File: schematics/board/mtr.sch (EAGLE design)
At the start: 6 parts

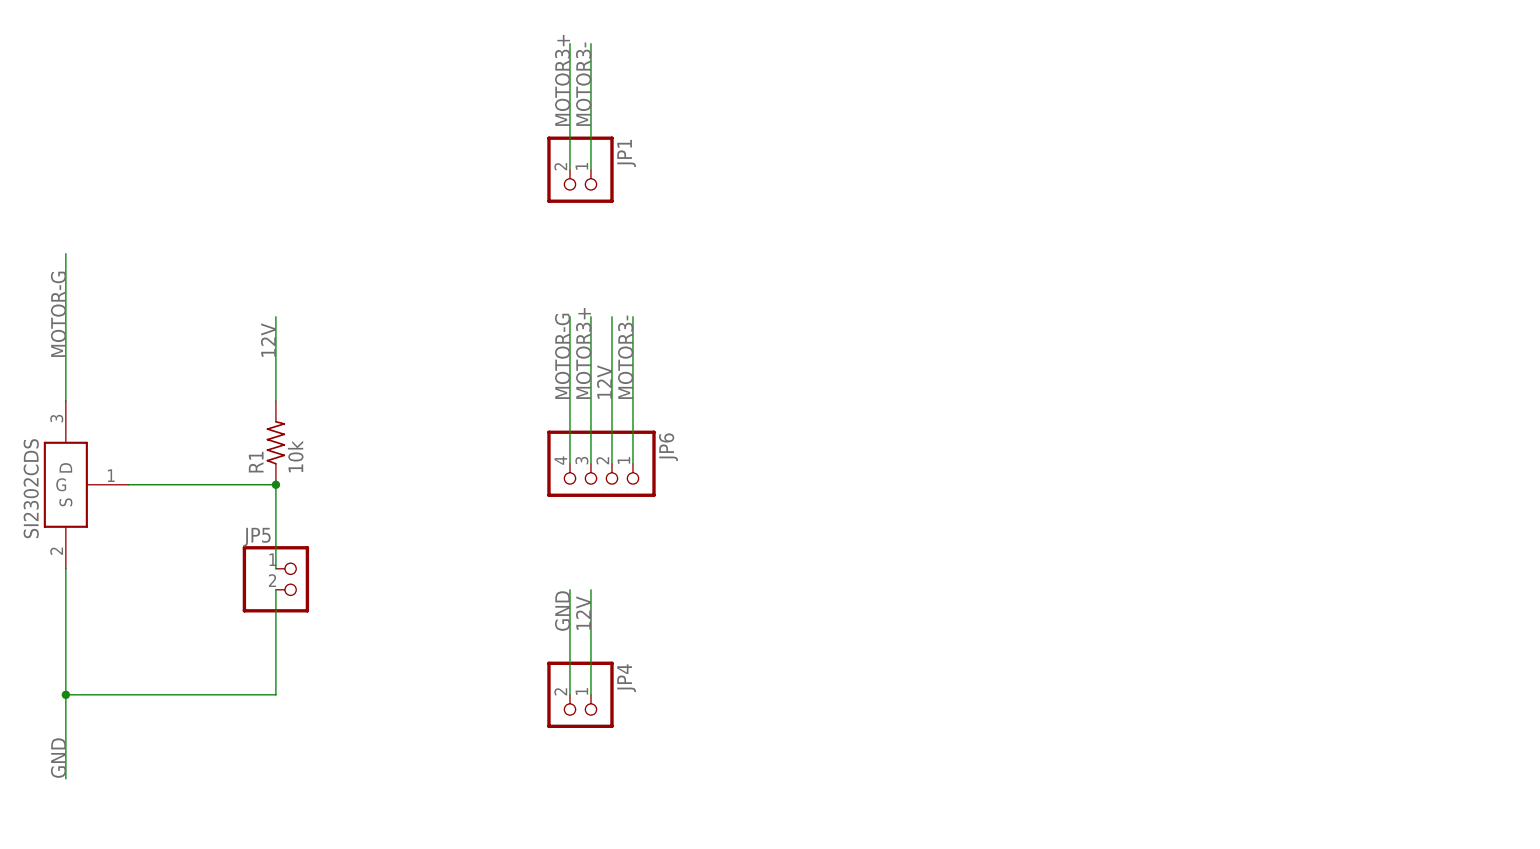
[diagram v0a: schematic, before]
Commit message: Доделаны платы dop и mtr
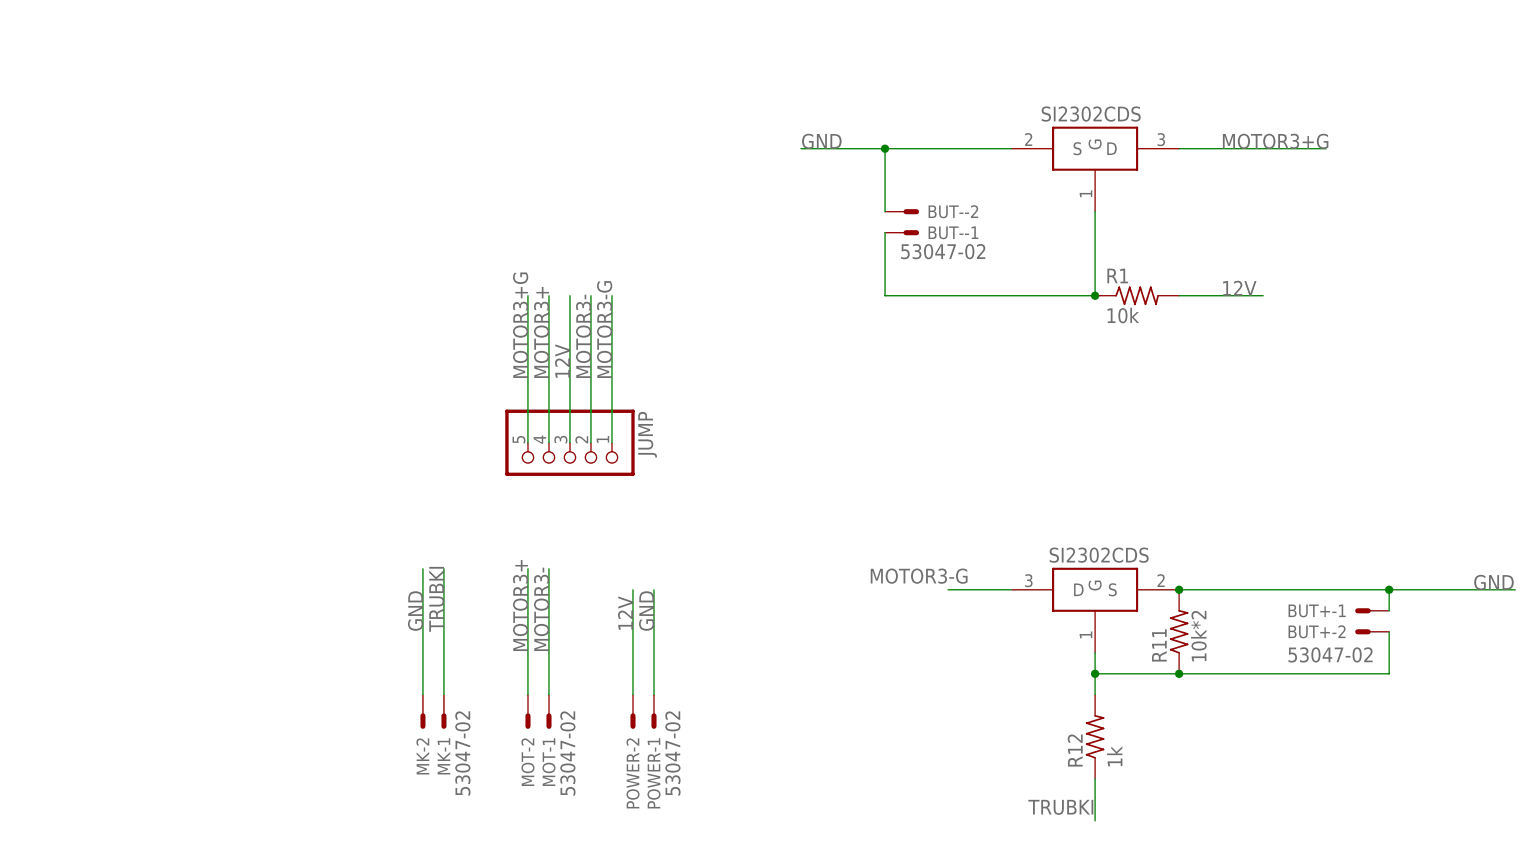
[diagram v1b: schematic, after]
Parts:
- removed JP1, JP4, JP5: (no value), pinhead:PINHD-1X2
- removed JP6: (no value), pinhead:PINHD-1X4
- added BUT+, BUT-, MK, MOT, POWER: 53047-02, con-molex:53047-02
- added JUMP: (no value), pinhead:PINHD-1X5
- added R11: 10k*2, rcl:R-US_R0603
- added R12: 1k, rcl:R-US_R0603
- added U$1: SI2302CDS, CanCubeSat:SI2302CDS
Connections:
- removed net MOTOR-G: JP6.4, U$21.D
- new net MOTOR3+G: JUMP.5, U$21.D
- new net MOTOR3-G: JUMP.1, U$1.D
- new net N$17: BUT+-2.S, R11.1, R12.2, U$1.G
- new net TRUBKI: MK-1.S, R12.1
- net 12V: now also JUMP.3, POWER-2.S; no longer JP4.1, JP6.2
- net GND: now also BUT+-1.S, BUT--2.S, MK-2.S, POWER-1.S, R11.2, U$1.S; no longer JP4.2, JP5.2
- net MOTOR3+: now also JUMP.4, MOT-2.S; no longer JP1.2, JP6.3
- net MOTOR3-: now also JUMP.2, MOT-1.S; no longer JP1.1, JP6.1
- net N$1: now also BUT--1.S; no longer JP5.1
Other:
- moved on the sheet: R1
